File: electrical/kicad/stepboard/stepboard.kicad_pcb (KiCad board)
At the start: 2 copper layers, 142.2 x 77.5 mm, 76 parts, among them J1 Conn_02x03_Odd_Even, J10 Conn_02x03_Odd_Even, J11 Conn_02x03_Odd_Even, J12 Conn_02x03_Odd_Even, J13 Conn_01x04, J14 Conn_01x04, J15 Conn_01x04, J16 Conn_01x04, J17 Conn_01x04, J18 Conn_01x04, J19 Conn_01x04, J2 Conn_02x03_Odd_Even, J20 Conn_01x04, J21 Conn_01x04, J22 Conn_01x04, J23 Conn_01x04, J24 Conn_01x04, J25 Conn_02x18_Odd_Even, J26 Screw_Terminal_01x03, J3 Conn_02x03_Odd_Even, J4 Conn_02x03_Odd_Even, J5 Conn_02x03_Odd_Even, J6 Conn_02x03_Odd_Even, J7 Conn_02x03_Odd_Even, J8 Conn_02x03_Odd_Even, J9 Conn_02x03_Odd_Even, U1 MKS_TMC2209, U10 MKS_TMC2209, U11 MKS_TMC2209, U12 MKS_TMC2209, U2 MKS_TMC2209, U3 MKS_TMC2209, U4 MKS_TMC2209, U5 MKS_TMC2209, U6 MKS_TMC2209, U7 MKS_TMC2209, U8 MKS_TMC2209, U9 MKS_TMC2209

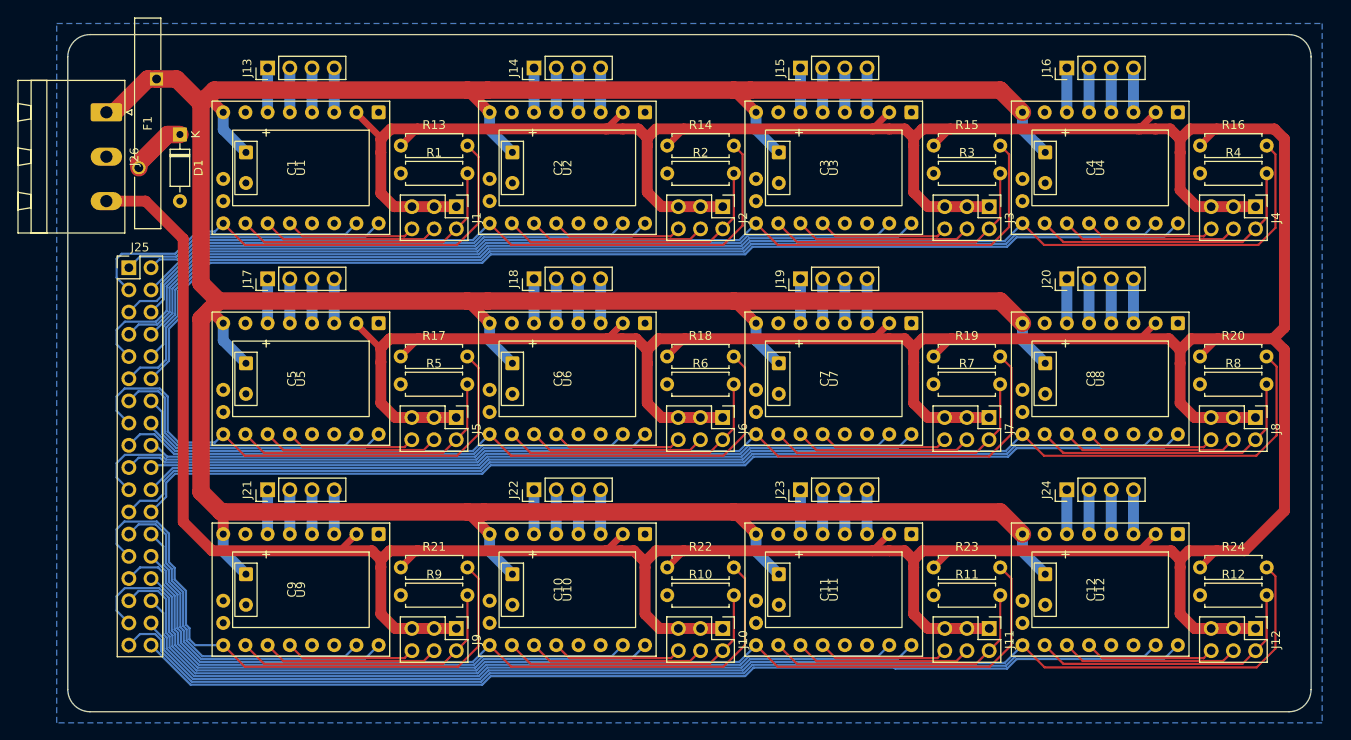
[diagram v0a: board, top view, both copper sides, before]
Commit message: update(kicad/step): adjust tolerances for PCB Machining
- Minimum track width: 0.3mm and Minimum track spacing: 0.2mm
- Added Teardrops for all pads
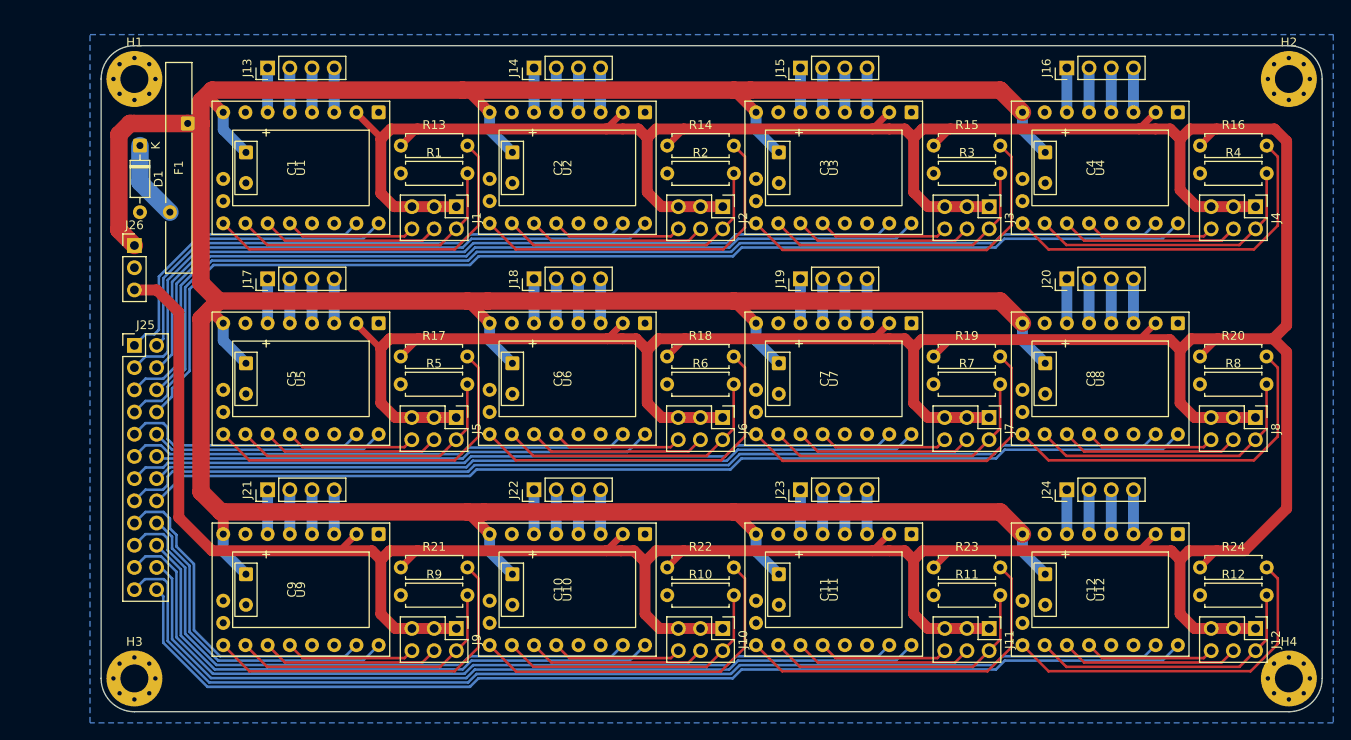
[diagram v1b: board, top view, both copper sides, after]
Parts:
- added H1: MountingHole_Pad, MountingHole:MountingHole_3.2mm_M3_Pad_Via, F.Cu at (25.4, 30.5)
- added H2: MountingHole_Pad, MountingHole:MountingHole_3.2mm_M3_Pad_Via, F.Cu at (157.5, 30.5)
- added H3: MountingHole_Pad, MountingHole:MountingHole_3.2mm_M3_Pad_Via, F.Cu at (25.4, 99.1)
- added H4: MountingHole_Pad, MountingHole:MountingHole_3.2mm_M3_Pad_Via, F.Cu at (157.5, 99.1)
- J25: value Conn_02x18_Odd_Even -> Conn_02x12_Odd_Even; footprint Connector_PinHeader_2.54mm:PinHeader_2x18_P2.54mm_Vertical -> Connector_PinHeader_2.54mm:PinHeader_2x12_P2.54mm_Vertical
- J26: footprint Connector_Phoenix_MSTB:PhoenixContact_MSTBA_2,5_3-G-5,08_1x03_P5.08mm_Horizontal -> Connector_PinHeader_2.54mm:PinHeader_1x03_P2.54mm_Vertical
- moved J26 15.6 mm to (25.4, 49.5), turned to 0 degrees
- moved J25 8.91 mm to (25.4, 61.0)
- moved F1 6.20 mm to (30.5, 40.6)
- moved D1 4.75 mm to (26.0, 38.1)
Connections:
- net /+5V renamed +5V
- net /GND renamed GND
- J25 pad 10: /ST4_ENA -> /ST5_DIR
- J25 pad 11: /ST4_STP -> /ST6_STP
- J25 pad 12: /ST4_DIR -> /ST6_DIR
- J25 pad 13: /ST5_STP -> /ST7_STP
- J25 pad 14: /ST5_DIR -> /ST7_DIR
- J25 pad 15: /ST5_ENA -> /ST8_STP
- J25 pad 16: /ST6_ENA -> /ST8_DIR
- J25 pad 17: /ST6_STP -> /ST9_STP
- J25 pad 18: /ST6_DIR -> /ST9_DIR
- J25 pad 19: /ST7_STP -> /ST10_STP
- J25 pad 20: /ST7_DIR -> /ST10_DIR
- J25 pad 21: /ST7_ENA -> /ST11_STP
- J25 pad 22: /ST8_ENA -> /ST11_DIR
- J25 pad 23: /ST8_STP -> /ST12_STP
- J25 pad 24: /ST8_DIR -> /ST12_DIR
- J25 pad 3: /ST1_ENA -> /ST2_STP
- J25 pad 4: /ST2_ENA -> /ST2_DIR
- J25 pad 5: /ST2_STP -> /ST3_STP
- J25 pad 6: /ST2_DIR -> /ST3_DIR
- J25 pad 7: /ST3_STP -> /ST4_STP
- J25 pad 8: /ST3_DIR -> /ST4_DIR
- J25 pad 9: /ST3_ENA -> /ST5_STP
- R13 pad 2: /ST1_ENA -> Net-(U1-~{EN})
- R14 pad 2: /ST2_ENA -> Net-(U2-~{EN})
- R15 pad 2: /ST3_ENA -> Net-(U3-~{EN})
- R16 pad 2: /ST4_ENA -> Net-(U4-~{EN})
- R17 pad 2: /ST5_ENA -> Net-(U5-~{EN})
- R18 pad 2: /ST6_ENA -> Net-(U6-~{EN})
- R19 pad 2: /ST7_ENA -> Net-(U7-~{EN})
- R20 pad 2: /ST8_ENA -> Net-(U8-~{EN})
- R21 pad 2: /ST9_ENA -> Net-(U9-~{EN})
- R22 pad 2: /ST10_ENA -> Net-(U10-~{EN})
- R23 pad 2: /ST11_ENA -> Net-(U11-~{EN})
- R24 pad 2: /ST12_ENA -> Net-(U12-~{EN})
- U1 pad 16: /ST1_ENA -> Net-(U1-~{EN})
- U10 pad 16: /ST10_ENA -> Net-(U10-~{EN})
- U11 pad 16: /ST11_ENA -> Net-(U11-~{EN})
- U12 pad 16: /ST12_ENA -> Net-(U12-~{EN})
- U2 pad 16: /ST2_ENA -> Net-(U2-~{EN})
- U3 pad 16: /ST3_ENA -> Net-(U3-~{EN})
- U4 pad 16: /ST4_ENA -> Net-(U4-~{EN})
- U5 pad 16: /ST5_ENA -> Net-(U5-~{EN})
- U6 pad 16: /ST6_ENA -> Net-(U6-~{EN})
- U7 pad 16: /ST7_ENA -> Net-(U7-~{EN})
- U8 pad 16: /ST8_ENA -> Net-(U8-~{EN})
- U9 pad 16: /ST9_ENA -> Net-(U9-~{EN})
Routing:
- net /ST4_ENA: track 149.5 -> 0.00 mm
- net /ST12_ENA: track 145.6 -> 0.00 mm
- net /ST8_ENA: track 142.9 -> 0.00 mm
- net /ST11_ENA: track 126.0 -> 0.00 mm
- net /ST3_ENA: track 124.0 -> 0.00 mm
- net /ST7_ENA: track 119.3 -> 0.00 mm
- net /ST10_ENA: track 89.0 -> 0.00 mm
- net /ST2_ENA: track 82.3 -> 0.00 mm
- net /ST6_ENA: track 82.1 -> 0.00 mm
- net /ST9_ENA: track 68.6 -> 0.00 mm
- net /ST5_ENA: track 62.2 -> 0.00 mm
- net /ST1_ENA: track 58.7 -> 0.00 mm
- net Net-(U2-~{EN}): track 0.00 -> 41.4 mm
- net Net-(U7-~{EN}): track 0.00 -> 41.3 mm
- net Net-(U3-~{EN}): track 0.00 -> 41.3 mm
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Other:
- board size 142.2 x 77.5 mm -> 139.7 x 76.2 mm
